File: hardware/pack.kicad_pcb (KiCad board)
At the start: 2 copper layers, 96 x 90 mm, 124 parts, among them U1 MT3608

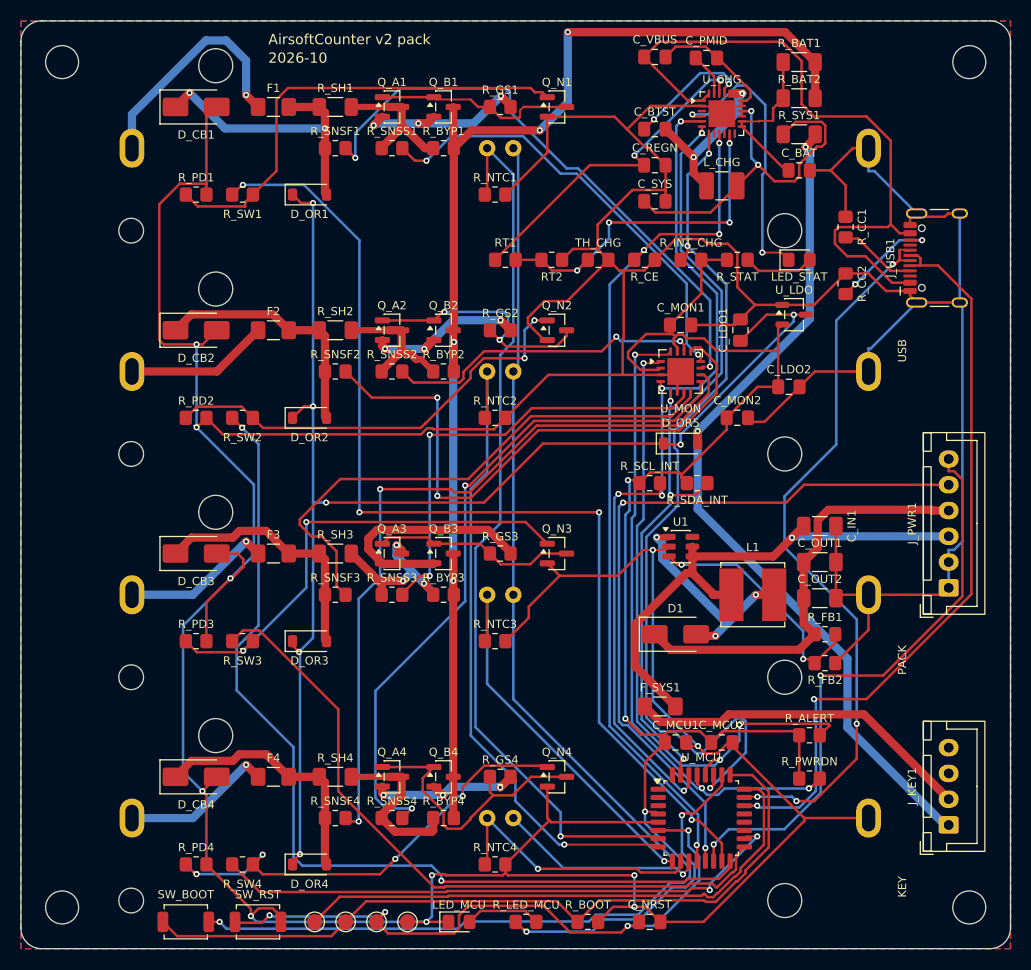
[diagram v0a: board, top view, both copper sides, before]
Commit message: hardware: off-board 2-wire connectors back to XH-2
J_HBAT1, J_BUZ1 and J_SPK1 (carrier) and J_KEY1 (pack) go back to JST-XH B2B-XH-A (C158012) instead of 4-pin B4B-XH-A (C144395) with pins 3-4 left no-connect. XH_SPARE is gone from both boards; the freed width puts J_BTN_R1 back on the carrier's top edge. Regenerated: both boards ERC/DRC clean, 0 unrouted.
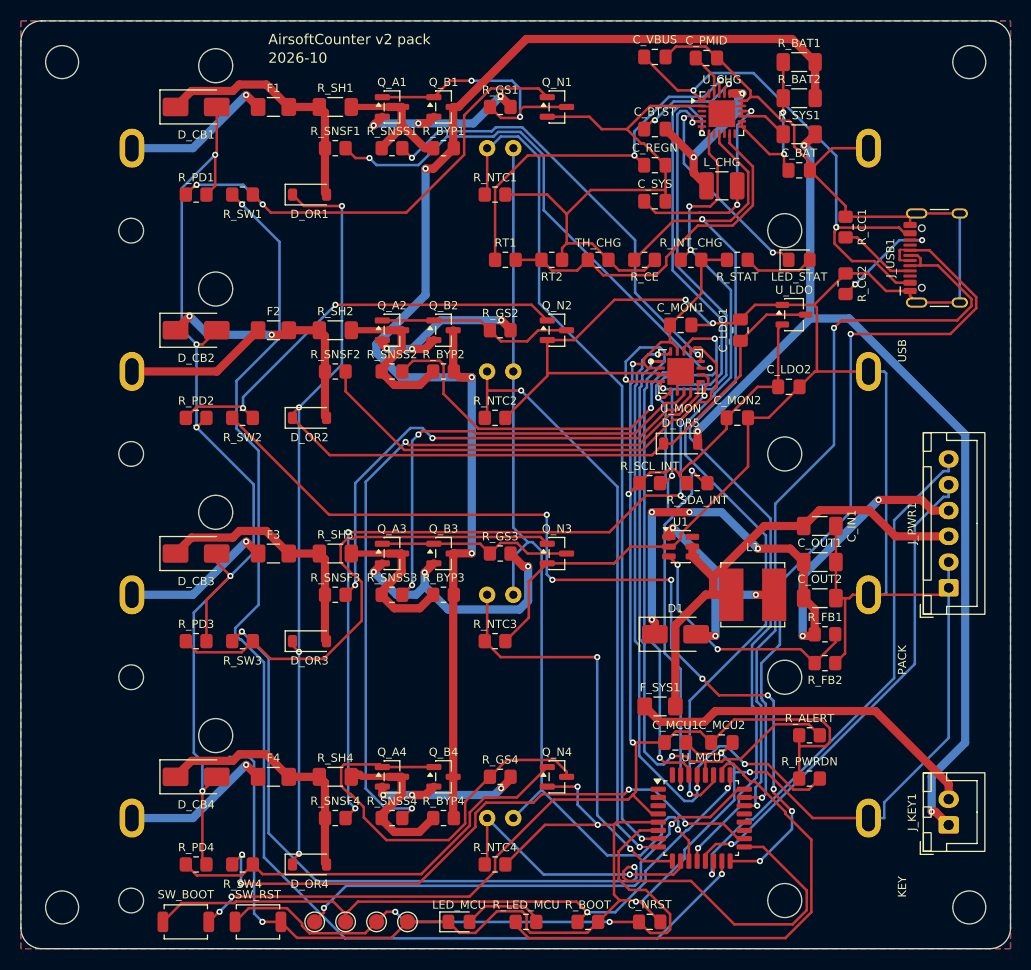
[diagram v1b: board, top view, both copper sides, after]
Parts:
- J_KEY1: footprint Connector_JST:JST_XH_B4B-XH-A_1x04_P2.50mm_Vertical -> Connector_JST:JST_XH_B2B-XH-A_1x02_P2.50mm_Vertical
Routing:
- net SW3_DRV: track 67.8 -> 92.6 mm, vias 0 -> 2
- net SDA_EXT: track 71.0 -> 47.7 mm, vias 2 -> 1
- net +5V: track 42.0 -> 60.8 mm, vias 0 -> 6
- net SW1_DRV: track 103.7 -> 122.5 mm, vias 4 -> 2
- net SCL_INT: track 84.1 -> 102.3 mm
- net LED_MCU_DRV: track 32.6 -> 50.3 mm, vias 2 -> 0
- net GND: track 581.4 -> 564.3 mm, vias 11 -> 13
- net SNS_S2: track 31.0 -> 46.1 mm
- net VBUS: track 65.4 -> 51.2 mm, vias 0 -> 2
- net SDA_INT: track 77.2 -> 90.6 mm
- net CELL4_G: track 28.1 -> 41.1 mm
- net SYS: track 83.6 -> 95.0 mm, vias 2 -> 3
- net CHG_CE: track 83.3 -> 93.4 mm, vias 4 -> 2
- net SYS_CHG: track 36.2 -> 27.5 mm
- net BOOT0: track 74.7 -> 66.2 mm, vias 0 -> 2
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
